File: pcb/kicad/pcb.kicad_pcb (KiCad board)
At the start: 2 copper layers, 303 x 103 mm, 85 parts, among them K0 KEYSW, K0A1 KEYSW, K0B1 KEYSW, K1 KEYSW, K10 KEYSW, K11 KEYSW, K12 KEYSW, K13 KEYSW, K14 KEYSW, K15 KEYSW, K16 KEYSW, K17 KEYSW, K18 KEYSW, K19 KEYSW, K1A1 KEYSW, K1B1 KEYSW, K2 KEYSW, K20 KEYSW, K21 KEYSW, K22 KEYSW, K23 KEYSW, K24 KEYSW, K25 KEYSW, K26 KEYSW, K27 KEYSW, K28 KEYSW, K29 KEYSW, K2A1 KEYSW, K2B1 KEYSW, K3 KEYSW, K33 KEYSW, K34 KEYSW, K35 KEYSW, K36 KEYSW, K37 KEYSW, K38 KEYSW, K4 KEYSW, K5 KEYSW, K6 KEYSW, K7 KEYSW, K8 KEYSW, K9 KEYSW, U1 Feather_32u4_BLE

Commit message: PCB: add v4 circuit board
- Split layout with Proton C and MCP 23017
- Sides can be connected with spring loaded pins or TRRS connectors
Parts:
- removed D0, D0A1, D0B1, D1, D16, D17, D18, D19, D1A1, D1B1, D2, D26, D27, D28, D29, D2A1, D2B1, D3, D36, D37, D38, D4, D5, D6, D7, D8, D9: D, Keyboard_Parts:D_SOD123_axial
- removed K0, K0A1, K0B1, K1, K16, K17, K18, K19, K1A1, K1B1, K2, K26, K27, K28, K29, K2A1, K2B1, K3, K36, K37, K38, K4, K5, K6, K7, K8, K9: KEYSW, Keebs:Mx_Alps_100
- removed U1: Feather_32u4_BLE, pcb:Feather_32u4_BLE
- added D00: D, Diode_SMD:D_SOD-323_HandSoldering, B.Cu at (-7.75, 44.0)
- added D01: D, Diode_SMD:D_SOD-323_HandSoldering, B.Cu at (11.2, 40.0)
- added D02: D, Diode_SMD:D_SOD-323_HandSoldering, B.Cu at (30.2, 36.0)
- added D03: D, Diode_SMD:D_SOD-323_HandSoldering, B.Cu at (49.2, 32.0)
- added D04: D, Diode_SMD:D_SOD-323_HandSoldering, B.Cu at (68.2, 36.0)
- added D05: D, Diode_SMD:D_SOD-323_HandSoldering, B.Cu at (87.2, 40.0)
- added D40: D, Diode_SMD:D_SOD-323_HandSoldering, B.Cu at (198.0, 40.0)
- added D41: D, Diode_SMD:D_SOD-323_HandSoldering, B.Cu at (216.8, 36.0)
- added D42: D, Diode_SMD:D_SOD-323_HandSoldering, B.Cu at (236.0, 31.9)
- added D43: D, Diode_SMD:D_SOD-323_HandSoldering, B.Cu at (254.8, 36.0)
- added D44: D, Diode_SMD:D_SOD-323_HandSoldering, B.Cu at (273.8, 40.0)
- added D45: D, Diode_SMD:D_SOD-323_HandSoldering, B.Cu at (292.8, 44.0)
- added D50: D, Diode_SMD:D_SOD-323_HandSoldering, B.Cu at (198.0, 59.0)
- added D51: D, Diode_SMD:D_SOD-323_HandSoldering, B.Cu at (216.8, 55.0)
- added D52: D, Diode_SMD:D_SOD-323_HandSoldering, B.Cu at (235.8, 51.0)
- added D53: D, Diode_SMD:D_SOD-323_HandSoldering, B.Cu at (255.0, 55.0)
- added D54: D, Diode_SMD:D_SOD-323_HandSoldering, B.Cu at (273.8, 59.0)
- added D55: D, Diode_SMD:D_SOD-323_HandSoldering, B.Cu at (293.0, 63.0)
- added D60: D, Diode_SMD:D_SOD-323_HandSoldering, B.Cu at (198.0, 78.0)
- added D61: D, Diode_SMD:D_SOD-323_HandSoldering, B.Cu at (217.0, 74.0)
- added D62: D, Diode_SMD:D_SOD-323_HandSoldering, B.Cu at (235.8, 70.0)
- added D63: D, Diode_SMD:D_SOD-323_HandSoldering, B.Cu at (254.8, 74.0)
- added D64: D, Diode_SMD:D_SOD-323_HandSoldering, B.Cu at (273.8, 78.0)
- added D65: D, Diode_SMD:D_SOD-323_HandSoldering, B.Cu at (293.0, 82.0)
- added D70: D, Diode_SMD:D_SOD-323_HandSoldering, B.Cu at (183.0, 116.0)
- added D71: D, Diode_SMD:D_SOD-323_HandSoldering, B.Cu at (197.8, 97.0)
- added D72: D, Diode_SMD:D_SOD-323_HandSoldering, B.Cu at (217.0, 93.0)
- added JLeft1: AudioJack5, 42_keyboard:Audio_Jack_5P_SMD_STX-3542, B.Cu at (125.8, 125.2)
- added JLeft2: Conn_01x04_Male, 42_keyboard:Conn-1x4, B.Cu at (131.9, 100.2)
- added JRight1: AudioJack5, 42_keyboard:Audio_Jack_5P_SMD_STX-3542, B.Cu at (169.2, 125.2)
- added JRight2: Conn_01x04_Female, 42_keyboard:Conn-1x4, B.Cu at (163.1, 107.8)
- added K00: KEYSW, keyswitches:Kailh_socket_MX_optional_custom, F.Cu at (-2.85, 50.1)
- added K01: KEYSW, keyswitches:Kailh_socket_MX_optional_custom, F.Cu at (16.1, 46.1)
- added K02: KEYSW, keyswitches:Kailh_socket_MX_optional_custom, F.Cu at (35.2, 42.1)
- added K03: KEYSW, keyswitches:Kailh_socket_MX_optional_custom, F.Cu at (54.2, 38.1)
- added K04: KEYSW, keyswitches:Kailh_socket_MX_optional_custom, F.Cu at (73.2, 42.1)
- added K05: KEYSW, keyswitches:Kailh_socket_MX_optional_custom, F.Cu at (92.2, 46.1)
- added K40: KEYSW, keyswitches:Kailh_socket_MX_optional_custom, F.Cu at (202.9, 46.0)
- added K41: KEYSW, keyswitches:Kailh_socket_MX_optional_custom, F.Cu at (221.8, 42.1)
- added K42: KEYSW, keyswitches:Kailh_socket_MX_optional_custom, F.Cu at (240.8, 38.1)
- added K43: KEYSW, keyswitches:Kailh_socket_MX_optional_custom, F.Cu at (259.8, 42.0)
- added K44: KEYSW, keyswitches:Kailh_socket_MX_optional_custom, F.Cu at (278.7, 46.1)
- added K45: KEYSW, keyswitches:Kailh_socket_MX_optional_custom, F.Cu at (297.8, 50.1)
- added K50: KEYSW, keyswitches:Kailh_socket_MX_optional_custom, F.Cu at (202.8, 65.2)
- added K51: KEYSW, keyswitches:Kailh_socket_MX_optional_custom, F.Cu at (221.8, 61.1)
- added K52: KEYSW, keyswitches:Kailh_socket_MX_optional_custom, F.Cu at (240.8, 57.2)
- added K53: KEYSW, keyswitches:Kailh_socket_MX_optional_custom, F.Cu at (259.9, 61.0)
- added K54: KEYSW, keyswitches:Kailh_socket_MX_optional_custom, F.Cu at (278.8, 65.2)
- added K55: KEYSW, keyswitches:Kailh_socket_MX_optional_custom, F.Cu at (297.9, 69.2)
- added K60: KEYSW, keyswitches:Kailh_socket_MX_optional_custom, F.Cu at (202.8, 84.2)
- added K61: KEYSW, keyswitches:Kailh_socket_MX_optional_custom, F.Cu at (221.8, 80.2)
- added K62: KEYSW, keyswitches:Kailh_socket_MX_optional_custom, F.Cu at (240.8, 76.0)
- added K63: KEYSW, keyswitches:Kailh_socket_MX_optional_custom, F.Cu at (259.8, 80.2)
- added K64: KEYSW, keyswitches:Kailh_socket_MX_optional_custom, F.Cu at (278.8, 84.2)
- added K65: KEYSW, keyswitches:Kailh_socket_MX_optional_custom, F.Cu at (297.9, 88.2)
- added K70: KEYSW, keyswitches:Kailh_socket_MX_optional_custom, F.Cu at (187.8, 122.2)
- added K71: KEYSW, keyswitches:Kailh_socket_MX_optional_custom, F.Cu at (202.8, 103.2)
- added K72: KEYSW, keyswitches:Kailh_socket_MX_optional_custom, F.Cu at (221.8, 99.0)
- added R1: R, Resistor_THT:R_Axial_DIN0204_L3.6mm_D1.6mm_P5.08mm_Horizontal, F.Cu at (180.0, 104.2)
- added R2: R, Resistor_THT:R_Axial_DIN0204_L3.6mm_D1.6mm_P5.08mm_Horizontal, F.Cu at (180.0, 100.5)
- added R3: R, Resistor_THT:R_Axial_DIN0204_L3.6mm_D1.6mm_P5.08mm_Horizontal, F.Cu at (175.0, 97.0)
- added ULeft1: proton_c_snapped, 42_keyboard:proton_c_snapped, F.Cu at (122.0, 56.0)
- added URight1: MCP23017_SP, Package_DIP:DIP-28_W7.62mm, F.Cu at (181.0, 88.8)
- D10, D11, D12, D13, D14, D15, D20, D21, D22, D23, D24, D25, D33, D34, D35: footprint Keyboard_Parts:D_SOD123_axial -> Diode_SMD:D_SOD-323_HandSoldering; moved to B.Cu
- K10, K11, K12, K13, K14, K15, K20, K21, K22, K23, K24, K25, K33, K34, K35: footprint Keebs:Mx_Alps_100 -> keyswitches:Kailh_socket_MX_optional_custom; moved to F.Cu
- moved K10 307.1 mm to (-2.85, 69.2), turned to 0 degrees
- moved K20 307.0 mm to (-2.75, 88.2), turned to 0 degrees
- moved D20 304.0 mm to (-7.75, 82.0), turned to 180 degrees
- moved D10 304.0 mm to (-7.75, 63.0), turned to 180 degrees
- moved K11 269.2 mm to (16.1, 65.2), turned to 0 degrees
- moved K21 269.1 mm to (16.2, 84.2), turned to 0 degrees
- moved D21 266.1 mm to (11.2, 78.0), turned to 180 degrees
- moved D11 266.1 mm to (11.2, 59.0), turned to 180 degrees
- moved K22 231.3 mm to (35.2, 80.2), turned to 0 degrees
- moved K12 231.3 mm to (35.2, 61.1), turned to 0 degrees
- moved D22 228.4 mm to (30.2, 74.0), turned to 180 degrees
- moved D12 228.4 mm to (30.2, 55.0), turned to 180 degrees
- moved K23 193.6 mm to (54.1, 76.2), turned to 0 degrees
- moved K13 193.5 mm to (54.2, 57.1), turned to 0 degrees
- moved D13 190.8 mm to (49.2, 51.0), turned to 180 degrees
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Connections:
- net /row1 renamed rowL1
- net /row2 renamed rowL2
- net /row3 renamed rowL3
- K10 pad 1: /col0 -> Net-(D10-Pad2)
- K10 pad 2: Net-(D10-Pad2) -> colL0
- K11 pad 1: /col1 -> Net-(D11-Pad2)
- K11 pad 2: Net-(D11-Pad2) -> colL1
- K12 pad 1: /col2 -> Net-(D12-Pad2)
- K12 pad 2: Net-(D12-Pad2) -> colL2
- K13 pad 1: /col3 -> Net-(D13-Pad2)
- K13 pad 2: Net-(D13-Pad2) -> colL3
- K14 pad 1: /col4 -> Net-(D14-Pad2)
- K14 pad 2: Net-(D14-Pad2) -> colL4
- K15 pad 1: /col5 -> Net-(D15-Pad2)
- K15 pad 2: Net-(D15-Pad2) -> colL5
- K20 pad 1: /col0 -> Net-(D20-Pad2)
- K20 pad 2: Net-(D20-Pad2) -> colL0
- K21 pad 1: /col1 -> Net-(D21-Pad2)
- K21 pad 2: Net-(D21-Pad2) -> colL1
- K22 pad 1: /col2 -> Net-(D22-Pad2)
- K22 pad 2: Net-(D22-Pad2) -> colL2
- K23 pad 1: /col3 -> Net-(D23-Pad2)
- K23 pad 2: Net-(D23-Pad2) -> colL3
- K24 pad 1: /col4 -> Net-(D24-Pad2)
- K24 pad 2: Net-(D24-Pad2) -> colL4
- K25 pad 1: /col5 -> Net-(D25-Pad2)
- K25 pad 2: Net-(D25-Pad2) -> colL5
- K33 pad 1: /col3 -> Net-(D33-Pad2)
- K33 pad 2: Net-(D33-Pad2) -> colL3
- K34 pad 1: /col4 -> Net-(D34-Pad2)
- K34 pad 2: Net-(D34-Pad2) -> colL4
- K35 pad 1: /col5 -> Net-(D35-Pad2)
- K35 pad 2: Net-(D35-Pad2) -> colL5
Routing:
- net /row0: track 365.8 -> 0.00 mm
- net rowL2: track 480.4 -> 159.3 mm, vias 2 -> 0
- net colL0: track 0.00 -> 309.6 mm, vias 0 -> 4
- net colL1: track 0.00 -> 254.9 mm, vias 0 -> 4
- net colL2: track 0.00 -> 243.3 mm, vias 0 -> 6
- net colL4: track 0.00 -> 240.1 mm, vias 0 -> 1
- net colL3: track 0.00 -> 239.4 mm, vias 0 -> 3
- net colL5: track 0.00 -> 233.0 mm
- net colR2: track 0.00 -> 225.1 mm, vias 0 -> 2
- net rowL1: track 373.1 -> 157.9 mm, vias 6 -> 0
- net colR1: track 0.00 -> 203.0 mm, vias 0 -> 2
- net colR4: track 0.00 -> 201.7 mm, vias 0 -> 1
- net colR5: track 0.00 -> 200.4 mm, vias 0 -> 2
- net /col0: track 184.9 -> 0.00 mm, vias 3 -> 0
- net colR3: track 0.00 -> 184.8 mm
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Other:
- board size 303 x 103 mm -> 320.5 x 103.9 mm
- board text added: "42.nglgzz.com"
- board text removed: "nglgzz 42"

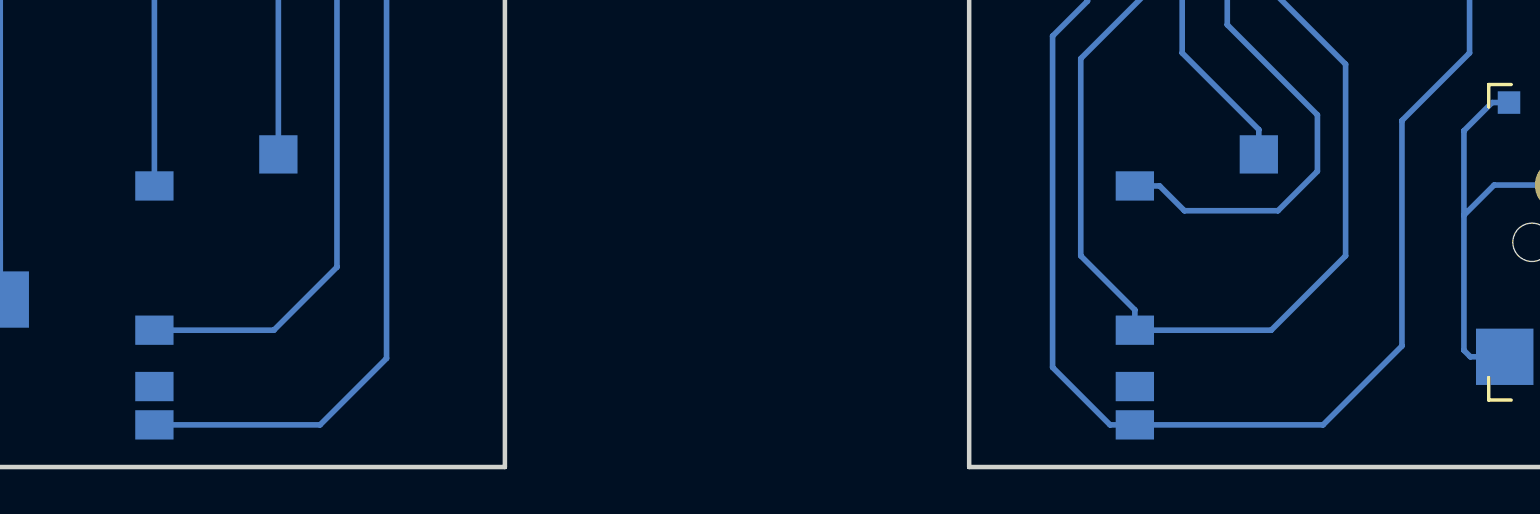
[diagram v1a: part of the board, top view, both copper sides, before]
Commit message: PCB: fix TRRS connectors position
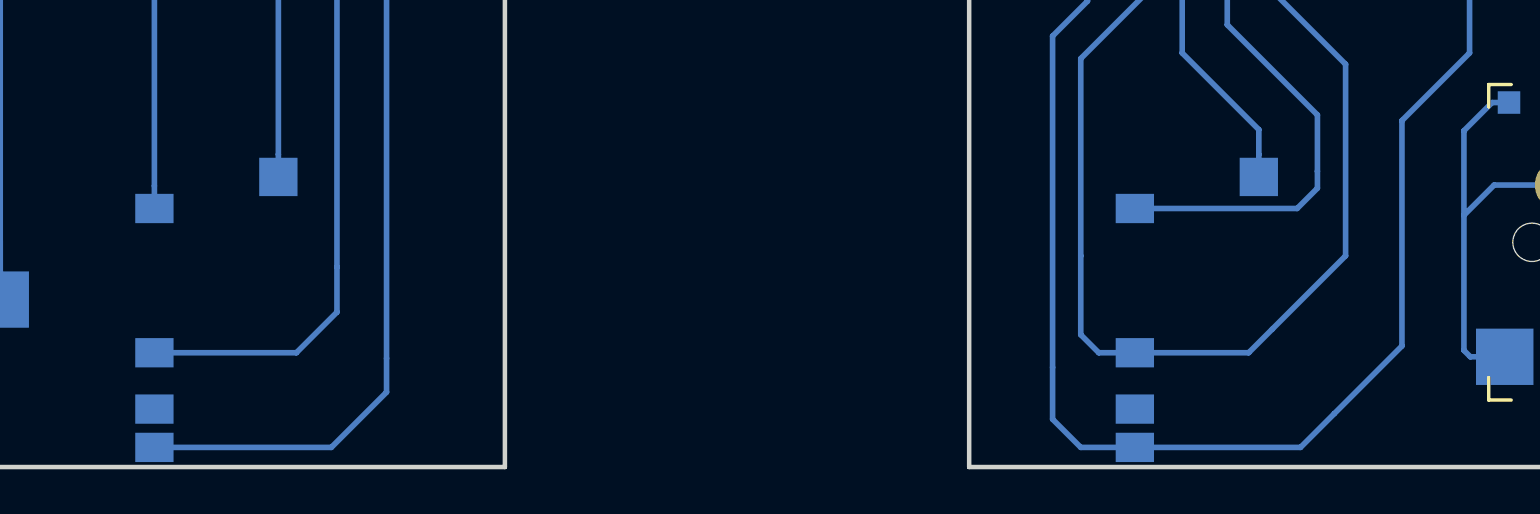
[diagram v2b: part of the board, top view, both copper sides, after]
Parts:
- moved JLeft1 1.00 mm to (125.8, 126.2)
- moved JRight1 1.00 mm to (169.2, 126.2)
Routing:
- net SDAR: track 105.2 -> 107.6 mm
- net +5vR: track 100.2 -> 102.4 mm
- net SDAL: track 99.8 -> 101.4 mm
- net +5vL: track 102.6 -> 103.9 mm
- net SCLR: track 74.4 -> 75.4 mm
- net SCLL: track 81.5 -> 82.5 mm
- net GND: track 88.7 -> 89.7 mm

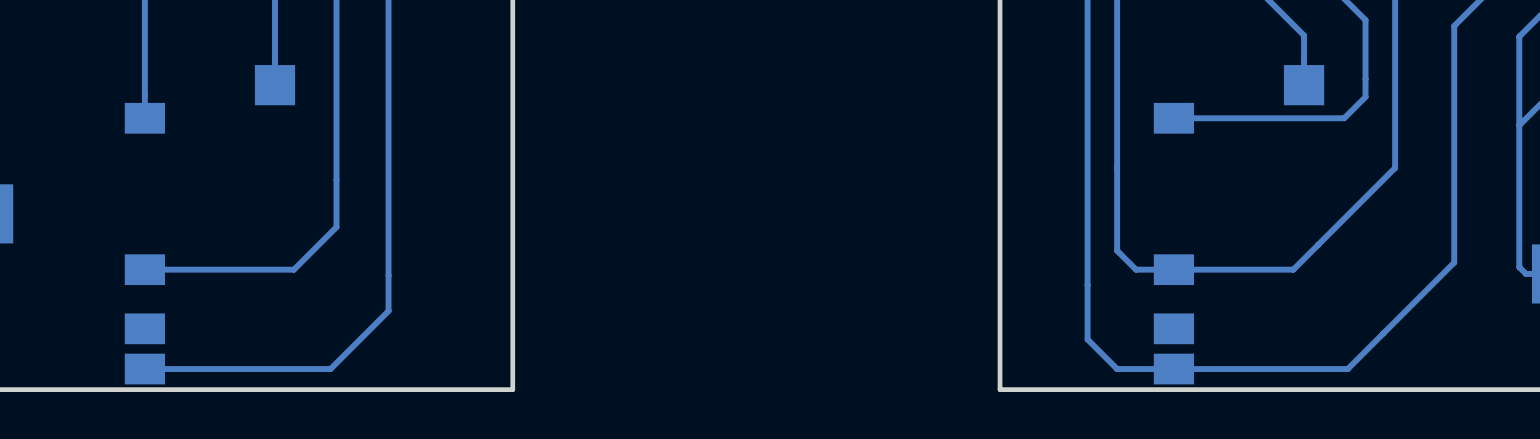
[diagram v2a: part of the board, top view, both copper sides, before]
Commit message: PCB: fix wiring of TRRS connectors
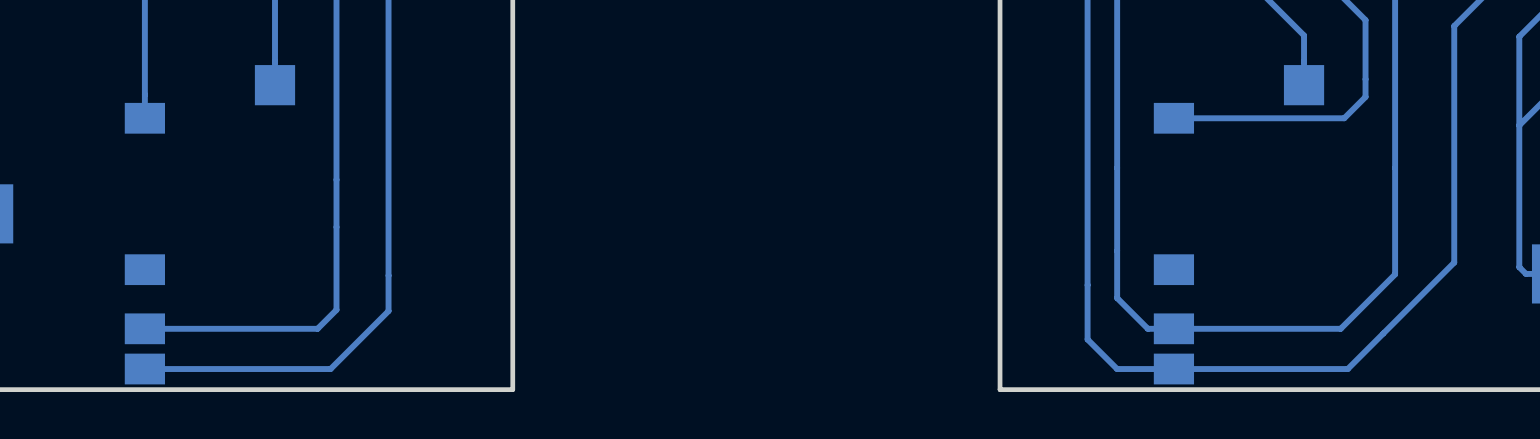
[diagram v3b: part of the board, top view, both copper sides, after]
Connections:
- JLeft1 pad 4: SDAL -> Net-(JLeft1-Pad4)
- JLeft1 pad 5: Net-(JLeft1-Pad5) -> SDAL
- JRight1 pad 4: SDAR -> Net-(JRight1-Pad4)
- JRight1 pad 5: Net-(JRight1-Pad5) -> SDAR
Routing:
- net SDAR: track 107.6 -> 113.5 mm
- net SDAL: track 101.4 -> 104.4 mm
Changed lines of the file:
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@@
   (general
     (thickness 1.6)
-    (drawings 54)
-    (tracks 1133)
+    (drawings 55)
+    (tracks 1135)
     (zones 0)
     (modules 93)
@@
     (solder_mask_min_width 0.25)
     (aux_axis_origin 0 0)
-    (visible_elements FFFFF7FF)
+    (visible_elements FFFFFFFF)
     (pcbplotparams
       (layerselection 0x010fc_ffffffff)
@@
   (net 91 "Net-(ULeft1-PadA9)")
   (net 92 "Net-(ULeft1-PadA10)")
-  (net 93 "Net-(JLeft1-Pad5)")
-  (net 94 "Net-(JRight1-Pad5)")
-  (net 95 GND)
+  (net 93 GND)
+  (net 94 "Net-(JLeft1-Pad4)")
+  (net 95 "Net-(JRight1-Pad4)")
   (net_class Default "This is the default net class."
     (clearance 0.2)
@@
     (add_net "Net-(D71-Pad2)")
     (add_net "Net-(D72-Pad2)")
-    (add_net "Net-(JLeft1-Pad5)")
-    (add_net "Net-(JRight1-Pad5)")
+    (add_net "Net-(JLeft1-Pad4)")
+    (add_net "Net-(JRight1-Pad4)")
     (add_net "Net-(R3-Pad1)")
     (add_net "Net-(ULeft1-Pad3.3V)")
@@
       (net 54 +5vR))
     (pad 5 smd rect (at -4.1 3.3) (size 1.7 1.3) (layers B.Cu B.Paste B.Mask)
-      (net 94 "Net-(JRight1-Pad5)"))
-    (pad 4 smd rect (at -4.1 0.8) (size 1.7 1.3) (layers B.Cu B.Paste B.Mask)
       (net 57 SDAR))
+    (pad 4 smd rect (at -4.1 0.8) (size 1.7 1.3) (layers B.Cu B.Paste B.Mask)
+      (net 95 "Net-(JRight1-Pad4)"))
     (pad 2 smd rect (at -4.1 -5.6) (size 1.7 1.3) (layers B.Cu B.Paste B.Mask)
       (net 55 GNDR))
@@
       (net 52 SCLL))
     (pad 1 thru_hole circle (at 0 0 270) (size 1.524 1.524) (drill 0.8128) (layers *.Cu *.Mask)
-      (net 95 GND))
+      (net 93 GND))
   )
   (module 42_keyboard:Conn-1x4 (layer B.Cu)
@@
       (net 90 "Net-(ULeft1-PadD+)"))
     (pad GND thru_hole circle (at -7.6 -10.17) (size 1.7 1.7) (drill 1) (layers *.Cu *.Mask)
-      (net 95 GND))
+      (net 93 GND))
     (pad GND thru_hole circle (at -7.6 -7.63) (size 1.7 1.7) (drill 1) (layers *.Cu *.Mask)
-      (net 95 GND))
+      (net 93 GND))
     (pad B7 thru_hole circle (at -7.6 -5.09) (size 1.7 1.7) (drill 1) (layers *.Cu *.Mask)
       (net 53 SDAL))
@@
       (net 23 rowL3))
     (pad GND thru_hole circle (at 7.615 -12.71) (size 1.7 1.7) (drill 1) (layers *.Cu *.Mask)
-      (net 95 GND))
+      (net 93 GND))
     (pad DFU thru_hole circle (at 7.615 -10.17) (size 1.7 1.7) (drill 1) (layers *.Cu *.Mask)
       (net 85 "Net-(ULeft1-PadDFU)"))
@@
       (net 51 +5vL))
     (pad 5 smd rect (at -4.1 3.3) (size 1.7 1.3) (layers B.Cu B.Paste B.Mask)
-      (net 93 "Net-(JLeft1-Pad5)"))
-    (pad 4 smd rect (at -4.1 0.8) (size 1.7 1.3) (layers B.Cu B.Paste B.Mask)
       (net 53 SDAL))
+    (pad 4 smd rect (at -4.1 0.8) (size 1.7 1.3) (layers B.Cu B.Paste B.Mask)
+      (net 94 "Net-(JLeft1-Pad4)"))
     (pad 2 smd rect (at -4.1 -5.6) (size 1.7 1.3) (layers B.Cu B.Paste B.Mask)
-      (net 95 GND))
+      (net 93 GND))
     (pad 3 smd rect (at 1.4 -7 270) (size 1.7 1.7) (layers B.Cu B.Paste B.Mask)
       (net 52 SCLL))
@@
   (segment (start 113.75 75.25) (end 120.75 75.25) (width 0.25) (layer F.Cu) (net 53))
   (segment (start 129.75 123.25) (end 129.75 125.25) (width 0.25) (layer B.Cu) (net 53))
-  (segment (start 127.95 127.05) (end 121.65 127.05) (width 0.25) (layer B.Cu) (net 53))
-  (segment (start 129.75 125.25) (end 127.95 127.05) (width 0.25) (layer B.Cu) (net 53))
+  (segment (start 129.75 125.25) (end 129.75 128.75) (width 0.25) (layer B.Cu) (net 53))
+  (segment (start 128.95 129.55) (end 121.65 129.55) (width 0.25) (layer B.Cu) (net 53))
+  (segment (start 129.75 128.75) (end 128.95 129.55) (width 0.25) (layer B.Cu) (net 53))
   (segment (start 161.5 127.7) (end 161.5 113) (width 0.25) (layer B.Cu) (net 54))
   (segment (start 163.05 111.45) (end 163.05 107.75) (width 0.25) (layer B.Cu) (net 54))
@@
   (segment (start 176.75 88.75) (end 176.75 98.67) (width 0.25) (layer F.Cu) (net 57))
   (segment (start 162.75 122.75) (end 162.75 126.25) (width 0.25) (layer B.Cu) (net 57))
-  (segment (start 163.55 127.05) (end 165.15 127.05) (width 0.25) (layer B.Cu) (net 57))
-  (segment (start 162.75 126.25) (end 163.55 127.05) (width 0.25) (layer B.Cu) (net 57))
-  (segment (start 170.2 127.05) (end 171.25 126) (width 0.25) (layer B.Cu) (net 57))
-  (segment (start 165.15 127.05) (end 170.2 127.05) (width 0.25) (layer B.Cu) (net 57))
-  (segment (start 171.25 126) (end 174.5 122.75) (width 0.25) (layer B.Cu) (net 57))
+  (segment (start 164.05 129.55) (end 165.15 129.55) (width 0.25) (layer B.Cu) (net 57))
+  (segment (start 162.75 128.25) (end 164.05 129.55) (width 0.25) (layer B.Cu) (net 57))
+  (segment (start 162.75 126.25) (end 162.75 128.25) (width 0.25) (layer B.Cu) (net 57))
+  (segment (start 165.15 129.55) (end 172.2 129.55) (width 0.25) (layer B.Cu) (net 57))
+  (segment (start 172.2 129.55) (end 174.5 127.25) (width 0.25) (layer B.Cu) (net 57))
+  (segment (start 174.5 127.25) (end 174.5 122.75) (width 0.25) (layer B.Cu) (net 57))
   (segment (start 4.71 50.09) (end 4.71 52.69) (width 0.25) (layer B.Cu) (net 58))
   (segment (start -0.31 45.07) (end 4.71 50.09) (width 0.25) (layer B.Cu) (net 58))
@@
   (segment (start 165.25 97) (end 175 97) (width 0.25) (layer B.Cu) (net 70))
   (segment (start 164 95.75) (end 165.25 97) (width 0.25) (layer B.Cu) (net 70))
-  (segment (start 121.65 119.65) (end 121.65 103.35) (width 0.25) (layer B.Cu) (net 95))
-  (segment (start 124.85 100.15) (end 131.95 100.15) (width 0.25) (layer B.Cu) (net 95))
-  (segment (start 121.65 103.35) (end 124.85 100.15) (width 0.25) (layer B.Cu) (net 95))
-  (segment (start 129.615 43.29) (end 135.5 49.175) (width 0.25) (layer B.Cu) (net 95))
-  (segment (start 135.5 49.175) (end 135.5 94.75) (width 0.25) (layer B.Cu) (net 95))
-  (segment (start 132 98.25) (end 132 99) (width 0.25) (layer B.Cu) (net 95))
-  (segment (start 135.5 94.75) (end 132 98.25) (width 0.25) (layer B.Cu) (net 95))
-  (segment (start 132 99) (end 131.95 100.15) (width 0.25) (layer B.Cu) (net 95))
-  (segment (start 121.65 119.65) (end 121.65 120.65) (width 0.25) (layer B.Cu) (net 95))
+  (segment (start 121.65 119.65) (end 121.65 103.35) (width 0.25) (layer B.Cu) (net 93))
+  (segment (start 124.85 100.15) (end 131.95 100.15) (width 0.25) (layer B.Cu) (net 93))
+  (segment (start 121.65 103.35) (end 124.85 100.15) (width 0.25) (layer B.Cu) (net 93))
+  (segment (start 129.615 43.29) (end 135.5 49.175) (width 0.25) (layer B.Cu) (net 93))
+  (segment (start 135.5 49.175) (end 135.5 94.75) (width 0.25) (layer B.Cu) (net 93))
+  (segment (start 132 98.25) (end 132 99) (width 0.25) (layer B.Cu) (net 93))
+  (segment (start 135.5 94.75) (end 132 98.25) (width 0.25) (layer B.Cu) (net 93))
+  (segment (start 132 99) (end 131.95 100.15) (width 0.25) (layer B.Cu) (net 93))
+  (segment (start 121.65 119.65) (end 121.65 120.65) (width 0.25) (layer B.Cu) (net 93))
 )
